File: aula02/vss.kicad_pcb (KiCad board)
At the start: 2 copper layers, 58 x 65 mm, 28 parts, among them J1 BATTERY, P1 MOTOR_L, P2 MOTOR_R, SW1 SW_SPST, U1 NUCLEO-F303K8, U2 SN754410, U3 LM78L05, U4 nRF24L01+

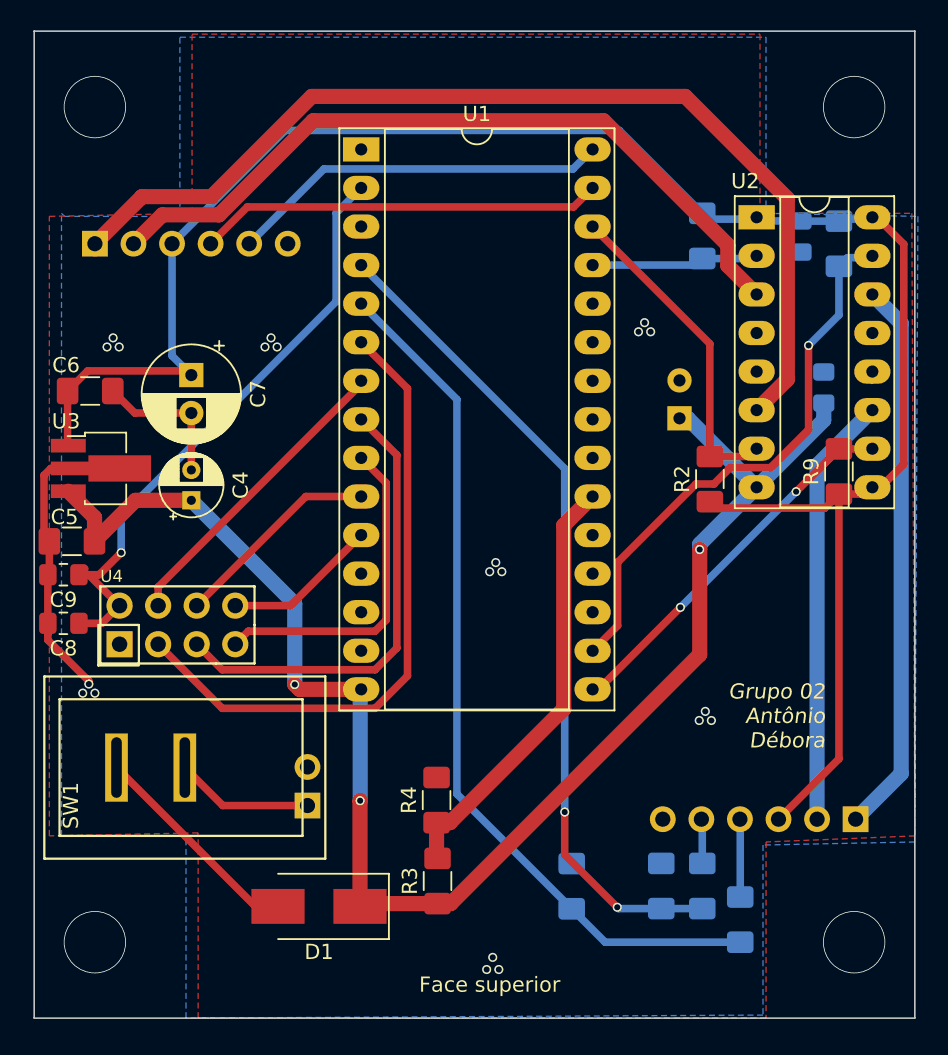
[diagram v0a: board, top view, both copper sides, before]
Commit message: fix: posicao capacitor e planos de ground
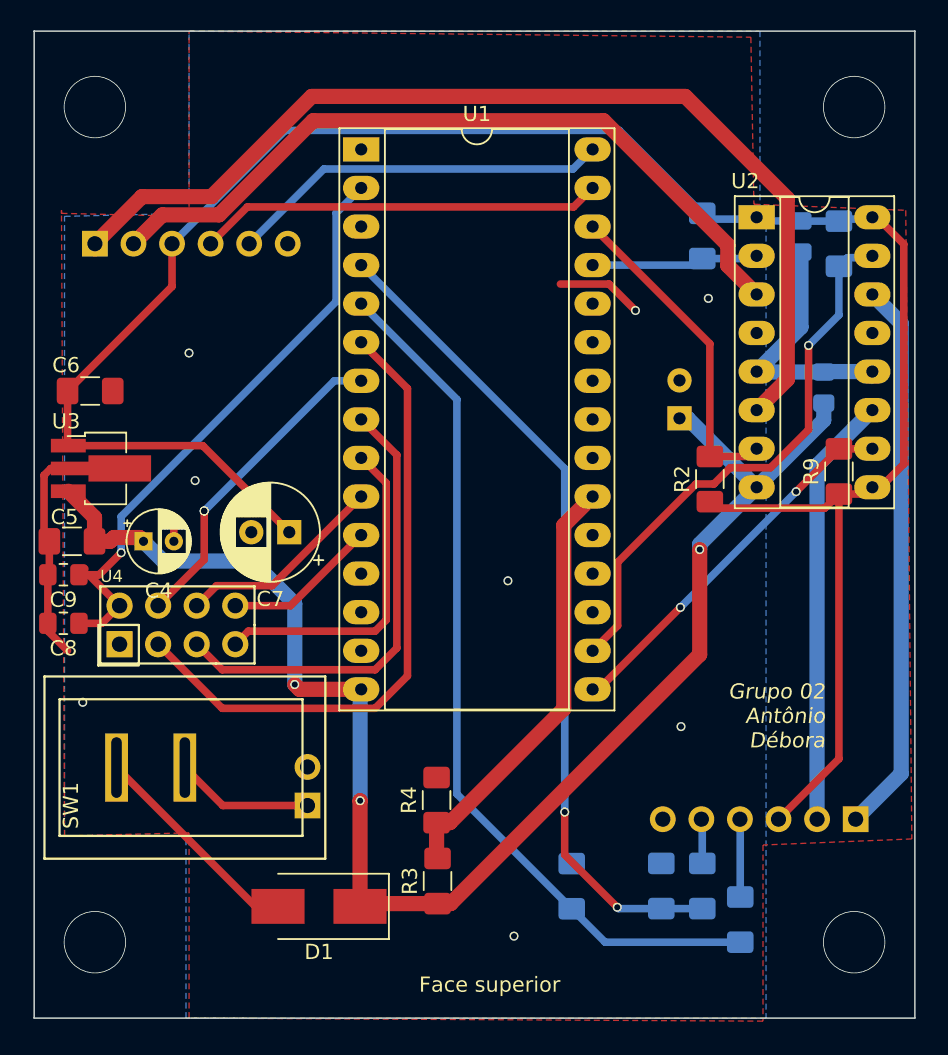
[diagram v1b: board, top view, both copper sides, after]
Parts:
- moved C7 12.2 mm to (136.8, 103.0), turned to 180 degrees
- moved C4 4.15 mm to (127.2, 103.6), turned to 0 degrees
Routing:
- net +5V: track 127.8 -> 139.3 mm
- net GND: track 29.4 -> 40.0 mm, vias 21 -> 8
- net +BATT: track 102.8 -> 100.8 mm
- net /Radio/CSN: track 20.3 -> 21.4 mm, vias 0 -> 2

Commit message: fix: R9 location
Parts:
- moved R9 4.46 mm to (171.5, 103.2), turned to 180 degrees
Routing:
- net +5V: track 139.3 -> 149.5 mm
- net /MotorR/PWM_1: track 25.8 -> 28.5 mm, vias 2 -> 0

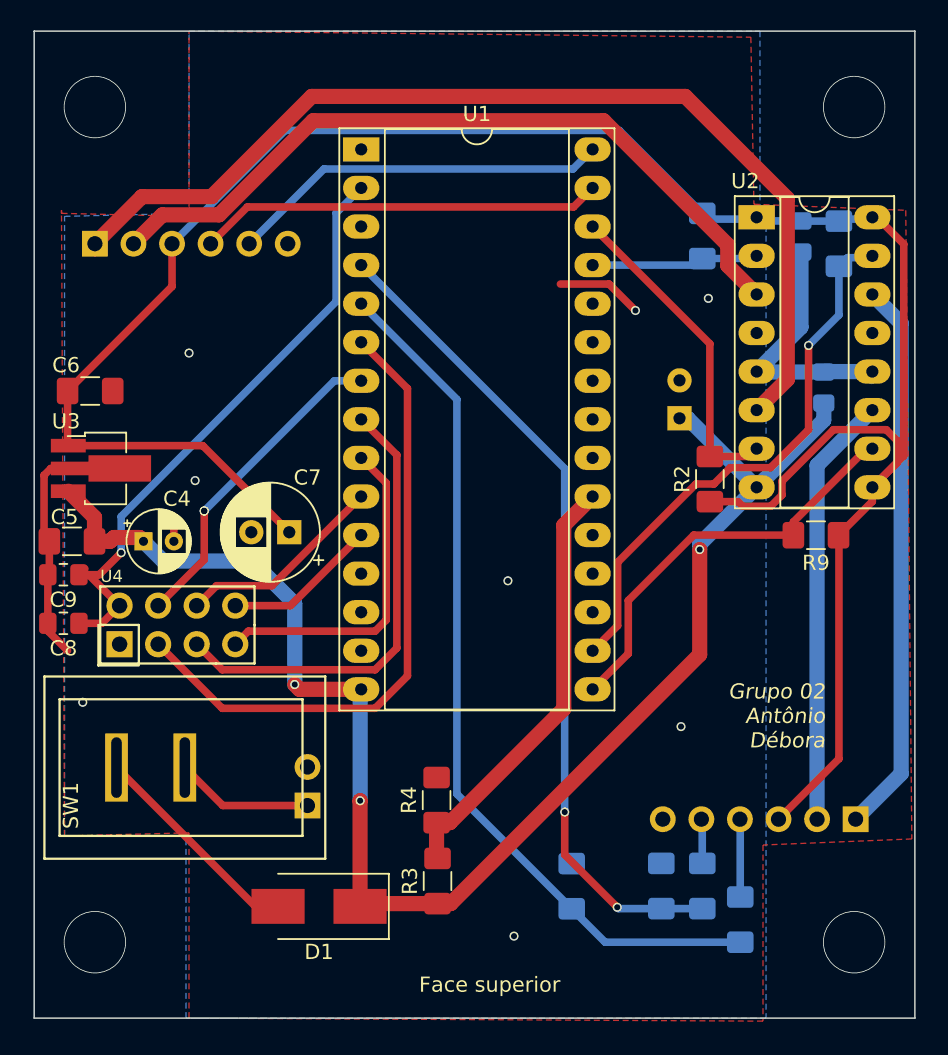
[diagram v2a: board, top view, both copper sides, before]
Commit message: fix: components under radio and filled zones
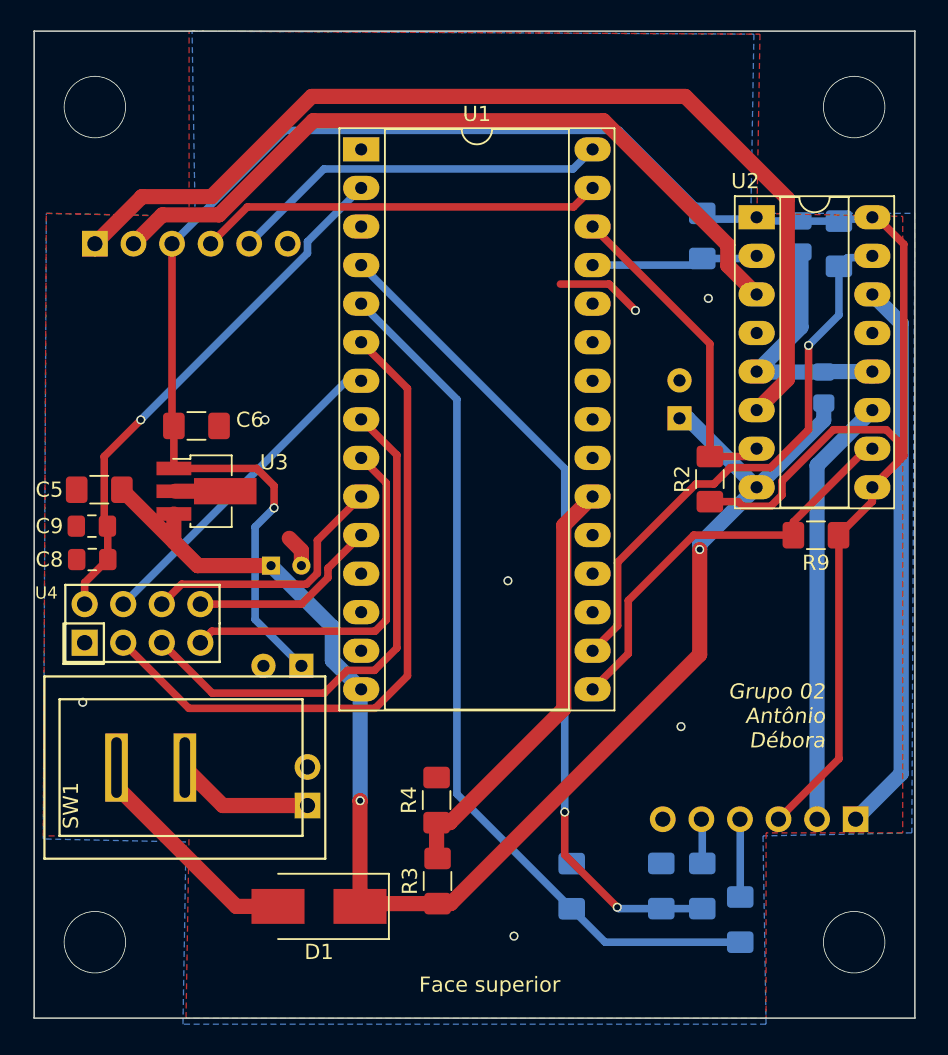
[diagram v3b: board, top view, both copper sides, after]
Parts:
- C4, C7: moved to B.Cu
- moved C7 8.84 mm to (137.6, 111.8)
- moved C4 8.55 mm to (135.6, 105.2)
- moved C6 7.37 mm to (130.7, 96.0)
- moved U3 7.11 mm to (131.3, 100.3)
- moved C8 4.61 mm to (123.8, 104.8)
- moved C5 3.85 mm to (124.3, 100.2)
- moved C9 3.71 mm to (123.8, 102.6)
- moved U4 2.30 mm to (121.8, 111.8)
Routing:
- net GND: track 40.0 -> 28.8 mm, vias 8 -> 7
- net +3V3: track 41.2 -> 35.1 mm
- net /Radio/SCK: track 30.5 -> 34.1 mm
- net /Radio/MOSI: track 13.8 -> 17.3 mm
- net /Radio/IRQ: track 10.2 -> 13.0 mm
- net +5V: track 149.5 -> 152.0 mm, vias 0 -> 1
- net +BATT: track 100.8 -> 98.4 mm, vias 3 -> 2
- net /Radio/CE: track 42.3 -> 44.6 mm
- net /Radio/MISO: track 22.0 -> 24.2 mm
- net Net-(D1-Pad2): track 14.4 -> 16.7 mm
- net /Radio/CSN: track 21.4 -> 21.8 mm, vias 2 -> 0
